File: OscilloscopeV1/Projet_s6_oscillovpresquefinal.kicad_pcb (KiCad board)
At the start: 2 copper layers, 34 parts, among them IC1 PGA849RGTR, J1 Conn_Coaxial, J2 Conn_01x06_Socket, J3 PILES_3AA, J4 Conn_01x05_Pin, SW1 SW_SPST, U1 MCP6001-OT, U2 AP2112K-3.3, U3 MCP1640x-xCHY, U4 STM32L476RGTx

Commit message: Ajout de toutes les empreintes
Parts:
- added C13: 10µ, Capacitor_SMD:CP_Elec_5x5.4, F.Cu at (185.4, 74.4)
- added C14: 10µ, Capacitor_SMD:CP_Elec_5x5.4, F.Cu at (185.4, 81.3)
- added C4: 10µ, Capacitor_SMD:CP_Elec_5x5.4, F.Cu at (185.4, 60.7)
- added C5: 10µ, Capacitor_SMD:CP_Elec_5x5.4, F.Cu at (185.4, 67.6)
- added D2: D_Zener, Diode_SMD:D_SOD-123, F.Cu at (192.8, 67.3)
- added D3: D_Schottky, Diode_SMD:D_SOD-123, F.Cu at (192.8, 70.6)
- added R2: 1,35k, Resistor_SMD:R_0815_2038Metric_Pad1.20x4.05mm_HandSolder, F.Cu at (192.3, 75.1)
- added U1: LM1117MP-5.0, Package_TO_SOT_SMD:SOT-223-3_TabPin2, F.Cu at (194.8, 61.5)
- SW1: footprint Button_Switch_THT:SW_Slide_SPDT_Straight_CK_OS102011MS2Q -> Connector_PinHeader_2.54mm:PinHeader_1x05_P2.54mm_Vertical
- renumbered U2 to U3
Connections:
- J3 pad 1: BAT_PLUS -> Net-(D3-A)
- SW1 pad 2: switch_Out -> Net-(D3-K)
- U3 pad 1: switch_Out -> BAT_PLUS
- U3 pad 3: switch_Out -> BAT_PLUS

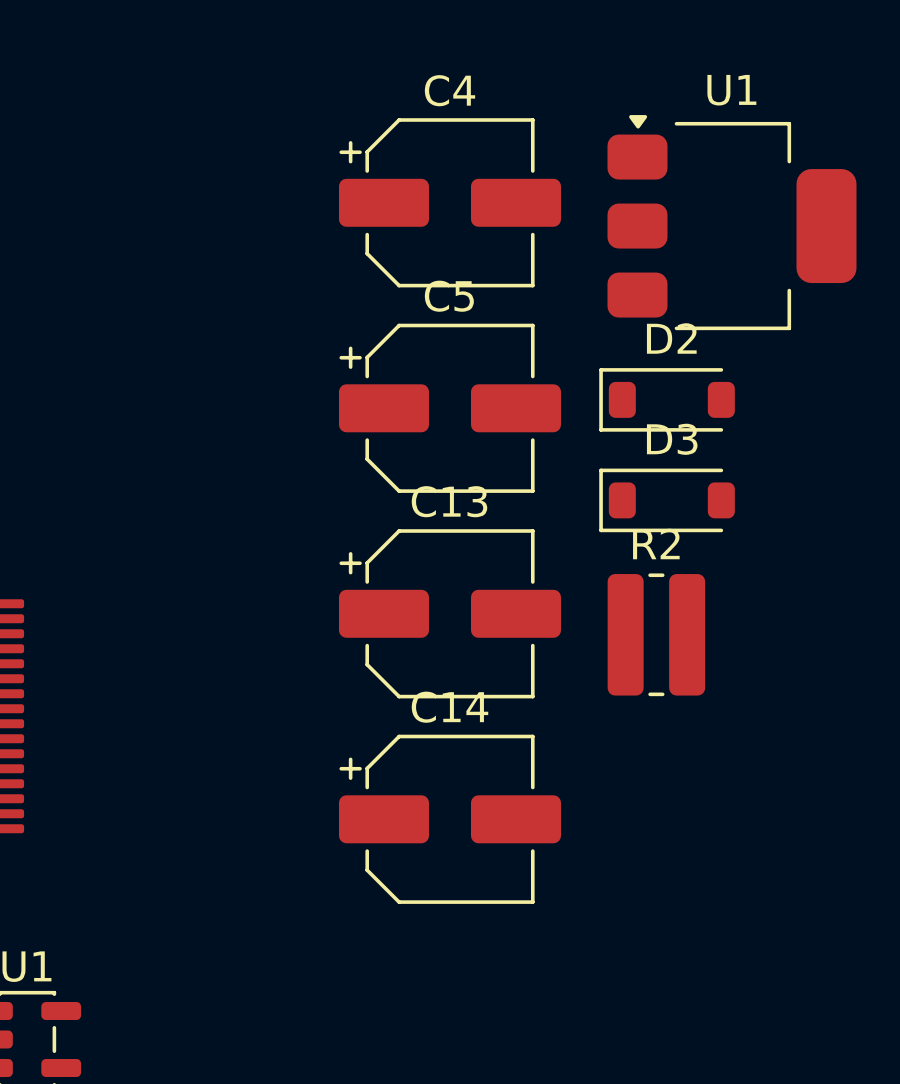
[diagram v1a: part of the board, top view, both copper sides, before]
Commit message: Finalisation Empreinte
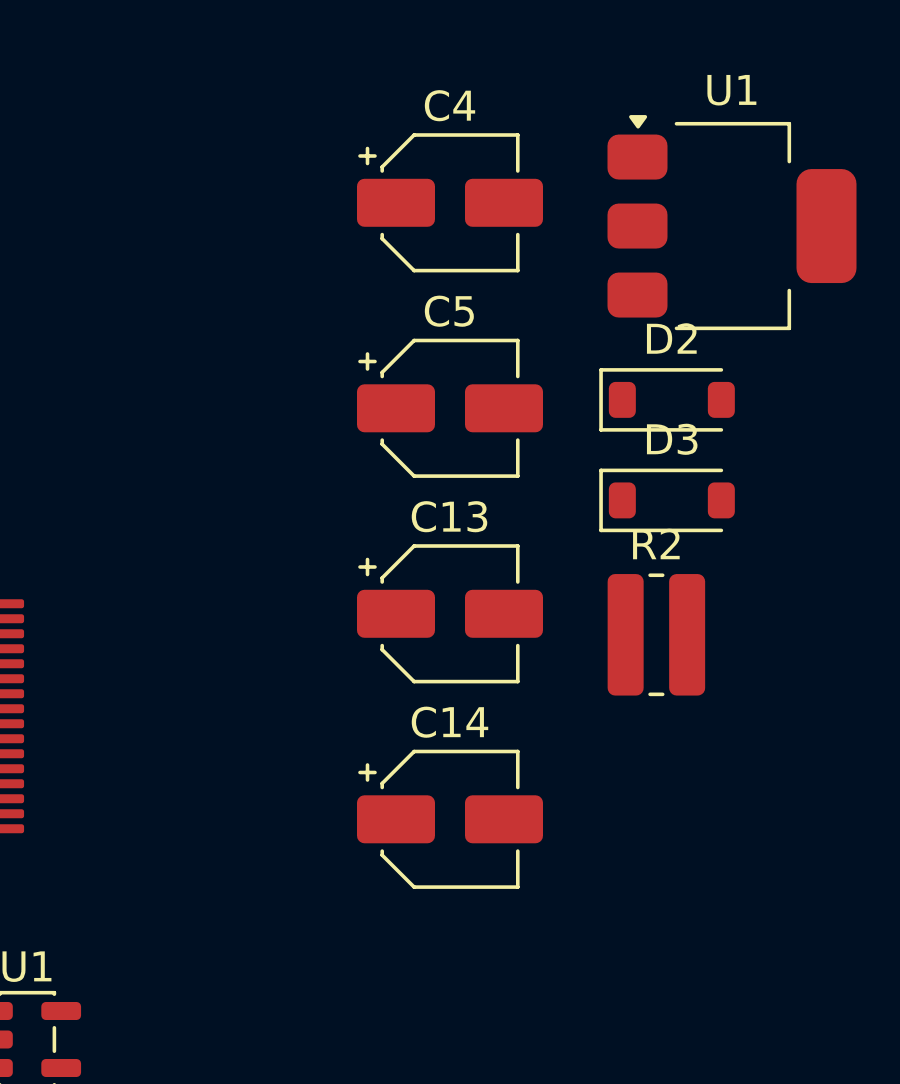
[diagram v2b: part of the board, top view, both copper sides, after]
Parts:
- C13, C14, C4, C5: footprint Capacitor_SMD:CP_Elec_5x5.4 -> Capacitor_SMD:CP_Elec_4x5.7

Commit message: Avancement PCB
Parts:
- removed SW1: SW_SPST, Connector_PinHeader_2.54mm:PinHeader_1x05_P2.54mm_Vertical
- added U1: MCP1826S, Package_TO_SOT_SMD:SOT-223, F.Cu at (175.8, 126.0)
- moved H4 70.1 mm to (180.0, 150.0)
- moved H3 63.9 mm to (153.0, 150.0)
- moved H2 60.6 mm to (180.0, 40.0)
- moved R2 48.4 mm to (144.0, 77.0)
- moved D2 46.0 mm to (148.0, 77.3), turned to 90 degrees
- moved D3 43.3 mm to (153.7, 89.0), turned to 180 degrees
- moved J4 41.0 mm to (177.0, 50.5)
- moved PS1 39.2 mm to (171.6, 110.0), turned to 90 degrees
- moved H1 37.1 mm to (150.0, 40.0)
- moved L1 36.6 mm to (148.0, 71.8), turned to 90 degrees
- moved IC1 31.9 mm to (144.5, 71.5)
- moved D1 31.4 mm to (152.9, 84.0)
- moved U1 31.2 mm to (165.8, 50.0)
- moved J1 29.0 mm to (139.0, 59.6)
- moved J3 27.9 mm to (139.0, 78.0)
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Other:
- board outline added: 53 x 74 mm

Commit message: Avancement PCB : Plans de masse et structuration
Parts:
- removed the C4 at (153.0, 95.0)
- removed the C5 at (164.0, 89.0)
- removed L1: 4,7µ, Inductor_SMD:L_0805_2012Metric_Pad1.05x1.20mm_HandSolder
- removed the R2 at (152.0, 75.0)
- removed R3: 9k, Resistor_SMD:R_0805_2012Metric_Pad1.20x1.40mm_HandSolder
- removed R4: 1k, Resistor_SMD:R_0805_2012Metric_Pad1.20x1.40mm_HandSolder
- removed R5: 300, Resistor_SMD:R_0805_2012Metric_Pad1.20x1.40mm_HandSolder
- removed the U1 at (165.8, 50.0)
- removed the U1 at (156.9, 72.9)
- removed the U3 at (156.9, 82.2)
- added SW1: SW_SPST, Connector_PinHeader_2.54mm:PinHeader_1x05_P2.54mm_Vertical, F.Cu at (190.1, 124.0)
- J1: footprint Connector_PinHeader_2.54mm:PinHeader_1x06_P2.54mm_Vertical -> Connector_Coaxial:BNC_TEConnectivity_1478204_Vertical
- J2: footprint Connector_Harwin:Harwin_M20-89006xx_1x06_P2.54mm_Horizontal -> Connector_PinSocket_2.54mm:PinSocket_1x06_P2.54mm_Horizontal
- moved J3 74.8 mm to (198.0, 124.0), turned to 180 degrees
- moved D3 53.0 mm to (194.0, 123.3), turned to -90 degrees
- moved D2 42.5 mm to (185.0, 56.4)
- moved R2 38.9 mm to (177.0, 56.4)
- moved C13 38.3 mm to (158.0, 102.2)
- moved C4 37.1 mm to (186.0, 117.0), turned to 0 degrees
- moved C2 32.2 mm to (167.0, 63.0), turned to 90 degrees
- moved C3 31.4 mm to (170.0, 63.0), turned to 90 degrees
- moved C5 29.2 mm to (151.0, 102.0)
- moved H4 29.1 mm to (200.0, 128.9)
- moved J2 27.8 mm to (190.6, 92.8), turned to 180 degrees
- moved U1 27.4 mm to (153.0, 110.8), turned to -90 degrees
- moved U3 27.4 mm to (166.9, 103.0)
- moved C1 26.1 mm to (164.0, 63.4), turned to -90 degrees
- moved H3 24.8 mm to (140.0, 128.9)
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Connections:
- J2 pad 5: Sortie5V_BOOST -> Sortie5V
- PS1 pad 3: Sortie5V_BOOST -> Sortie5V
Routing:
- added copper zone on B.Cu, net GND
- added copper zone on F.Cu, net GND
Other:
- board size 53 x 74 mm -> 66 x 84.4 mm

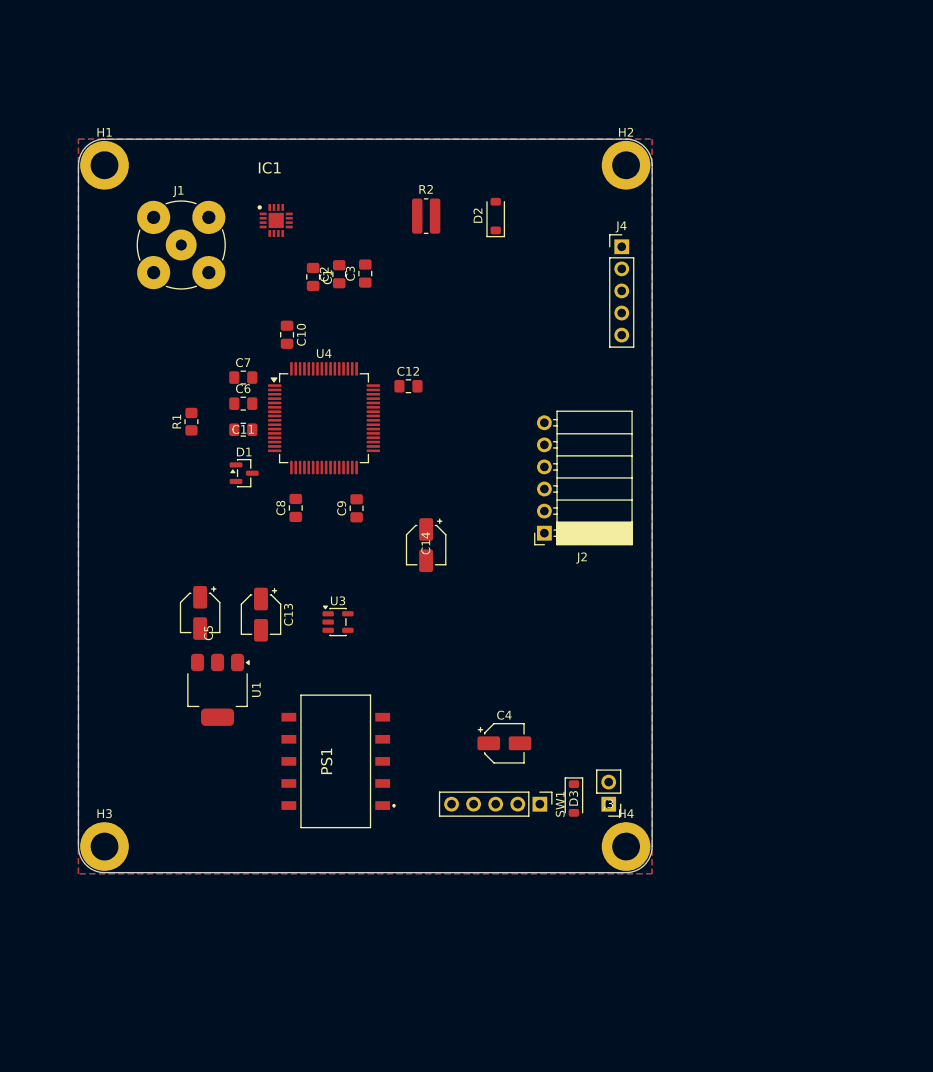
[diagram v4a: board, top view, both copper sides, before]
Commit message: Amincissement du pcb
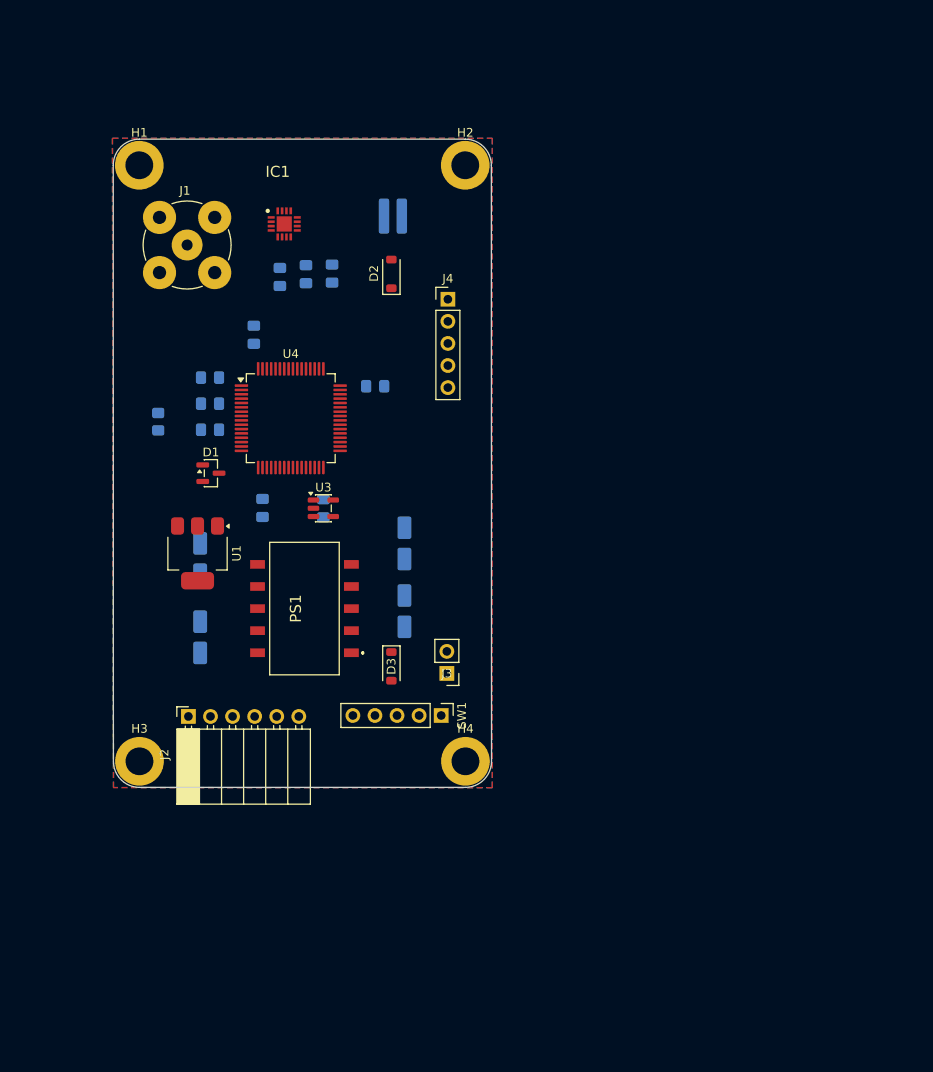
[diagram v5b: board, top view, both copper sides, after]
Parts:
- C1, C10, C11, C12, C13, C14, C2, C3, C4, C5, C6, C7, C8, C9, R1, R2: moved to B.Cu
- moved J2 46.1 mm to (149.7, 113.9), turned to 90 degrees
- moved D3 25.9 mm to (173.0, 108.2)
- moved J3 23.9 mm to (179.4, 109.0)
- moved H4 20.9 mm to (181.5, 119.1)
- moved J4 20.9 mm to (179.5, 65.9)
- moved C4 19.1 mm to (174.5, 101.8), turned to -90 degrees
- moved H2 18.5 mm to (181.5, 50.5)
- moved PS1 17.9 mm to (163.0, 101.5)
- moved U1 15.9 mm to (150.7, 95.2)
- moved SW1 15.3 mm to (178.7, 113.8)
- moved D2 13.7 mm to (173.0, 63.0)
- moved U3 13.2 mm to (165.2, 90.0)
- moved H3 10.6 mm to (144.0, 119.1)
- moved C13 7.47 mm to (151.0, 104.8)
- moved C5 6.20 mm to (151.0, 95.8)
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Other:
- board size 66 x 84.4 mm -> 43.5 x 74.6 mm

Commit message: Start routing (#2)
* Point de départ du routage

* Merge pull request #1 from YounesAchb/End-routing

Add files via upload

* Add files via upload

routage du pcb the long way

* PCB Final

---------

Co-authored-by: YounesAchb <younes.achbad@ensea.fr>
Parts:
- removed C4: 10µ, Capacitor_SMD:CP_Elec_4x5.7
- removed H3, H4: MountingHole_Pad, MountingHole:MountingHole_3.2mm_M3_DIN965_Pad
- C1, C10, C11, C12, C13, C14, C2, C3, C5, C6, C7, C8, C9, R1, R2: moved to F.Cu
- moved H1 86.3 mm to (229.4, 38.4)
- moved H2 82.2 mm to (213.3, 126.3)
- moved U1 81.0 mm to (228.1, 71.1), turned to 90 degrees
- moved C6 77.5 mm to (228.5, 91.5), turned to -90 degrees
- moved C13 77.1 mm to (223.4, 78.4), turned to 180 degrees
- moved C10 76.1 mm to (228.5, 96.7)
- moved PS1 76.0 mm to (224.3, 56.5)
- moved C7 73.7 mm to (225.3, 84.0)
- moved J1 73.4 mm to (220.4, 40.8)
- moved R1 72.9 mm to (218.8, 72.9)
- moved C8 71.9 mm to (230.1, 88.5), turned to 0 degrees
- moved D1 71.2 mm to (222.4, 73.9), turned to -90 degrees
- moved J2 68.8 mm to (218.3, 119.1)
- moved C5 64.9 mm to (213.5, 78.3)
- moved C11 62.7 mm to (214.7, 85.5), turned to 0 degrees
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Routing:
- net GND: track 0.00 -> 193.1 mm, vias 0 -> 5
- net V3.3_DIG: track 0.00 -> 119.0 mm, vias 0 -> 1
- net Sortie5V: track 0.00 -> 64.1 mm
- net Net-(IC1-IN-): track 0.00 -> 44.8 mm
- net BAT_PLUS: track 0.00 -> 41.1 mm, vias 0 -> 1
- net KEY: track 0.00 -> 37.4 mm, vias 0 -> 1
- net Net-(IC1-IN+): track 0.00 -> 28.8 mm
- net UART_TX: track 0.00 -> 24.4 mm, vias 0 -> 2
- net UART_RX: track 0.00 -> 24.0 mm, vias 0 -> 2
- net Entree_adc: track 0.00 -> 23.2 mm, vias 0 -> 2
- net Vref_1.5: track 0.00 -> 22.1 mm
- net ANL0: track 0.00 -> 21.9 mm, vias 0 -> 3
- net ANL1: track 0.00 -> 21.9 mm, vias 0 -> 2
- net ANL2: track 0.00 -> 21.0 mm, vias 0 -> 2
- net Traco_-15V: track 0.00 -> 20.2 mm
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- added copper zone on B.Cu, net (none)
- added copper zone on F.Cu, net (none)
- removed copper zone on B.Cu, net GND
- removed copper zone on F.Cu, net GND
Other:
- board size 43.5 x 74.6 mm -> 22.9 x 94.7 mm

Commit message: Add files via upload
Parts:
- moved J3 5.87 mm to (229.0, 113.9), turned to 180 degrees
- moved C7 2.13 mm to (227.4, 84.1), turned to 0 degrees
- moved C1 1.28 mm to (213.8, 67.5), turned to 90 degrees
- moved H1 0.22 mm to (229.3, 38.6)
- moved H2 0.18 mm to (213.4, 126.2)
- turned C12 to -90 degrees
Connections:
- C10 pad 2: V3.3_DIG -> GND
- C11 pad 2: V3.3_DIG -> GND
- C12 pad 2: V3.3_DIG -> GND
- C7 pad 2: V3.3_DIG -> GND
- C8 pad 2: V3.3_DIG -> GND
- C9 pad 2: V3.3_DIG -> GND
- R2 pad 1: Traco_+15V -> V3.3_DIG
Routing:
- net GND: track 193.1 -> 220.2 mm
- net ANL1: track 21.9 -> 27.4 mm
- net V3.3_DIG: track 119.0 -> 113.8 mm, vias 1 -> 4
- net Traco_+15V: track 19.7 -> 14.6 mm
- net ANL0: track 21.9 -> 25.6 mm
- net Net-(D3-A): track 12.3 -> 15.9 mm
- net ANL2: track 21.0 -> 24.7 mm
- net Sortie5V: track 64.1 -> 64.6 mm
